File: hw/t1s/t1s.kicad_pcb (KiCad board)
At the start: 4 copper layers, 58 x 11.8 mm, 18 parts, among them J1 SFP_Module_Edge, J2 2-pin T1S (JST PH placeholder), U1 LIFCL-17 CrossLink-NX csfBGA-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, U2 STM32G031F6P6 (I2C slave: EEP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, U3 TPS62A01 3V3->1V0, U4 LDO 3V3->1V8, U5 LAN8670 (MII), U6 SPI flash (FPGA bitstream), Y1 25 MHz

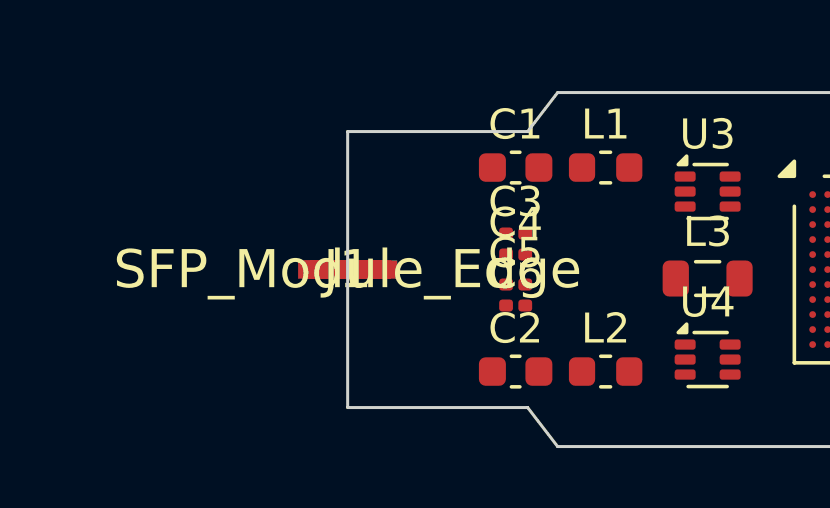
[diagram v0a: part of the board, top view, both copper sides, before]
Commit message: T1 module: schematic, routed 4-layer PCB, fab outputs, controller firmware
One netlist in make_t1.py drives both the schematic and the PCB pad nets;
the schematic's exported netlist matches it pin for pin (175 pins), and
eeschema's ERC is clean. Every block is from its datasheet: DP83TG720S
pins, straps, MDI network and decoupling; the DP83TC812S loadout differs
only in leaving FB3 off; TPS62821 1.0 V buck.

Routed by Freerouting 1.9.0 with In1 GND / In2 3V3 planes, outer GND
pours added after import, no pour among the gold fingers. KiCad DRC:
0 violations, 0 unconnected.

Firmware (STM32G031, 1.7 KB): A0h EEPROM emulation, I2C-to-MDIO bridge at
0x56 in the mdio-i2c protocol, TX_DISABLE holds the PHY in reset, RX_LOS
follows the link.

Not orderable yet: the H-MTD footprint is a placeholder and the SGMII
widths wait on the fab's stackup.
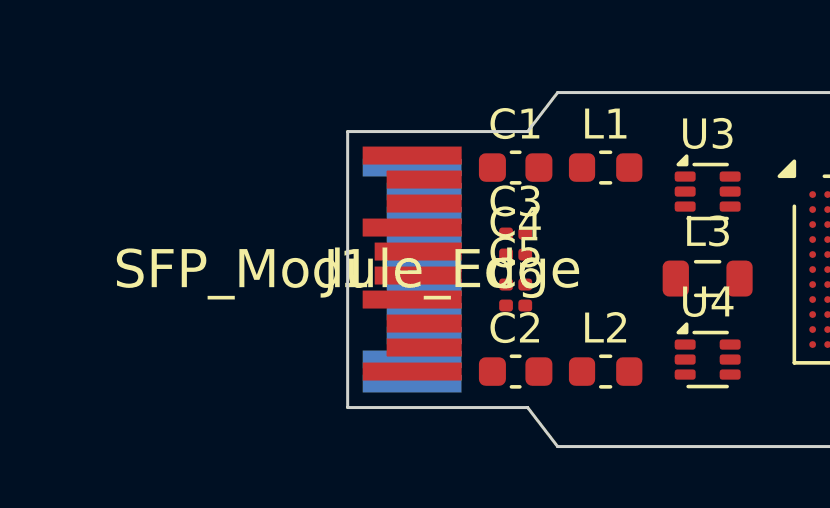
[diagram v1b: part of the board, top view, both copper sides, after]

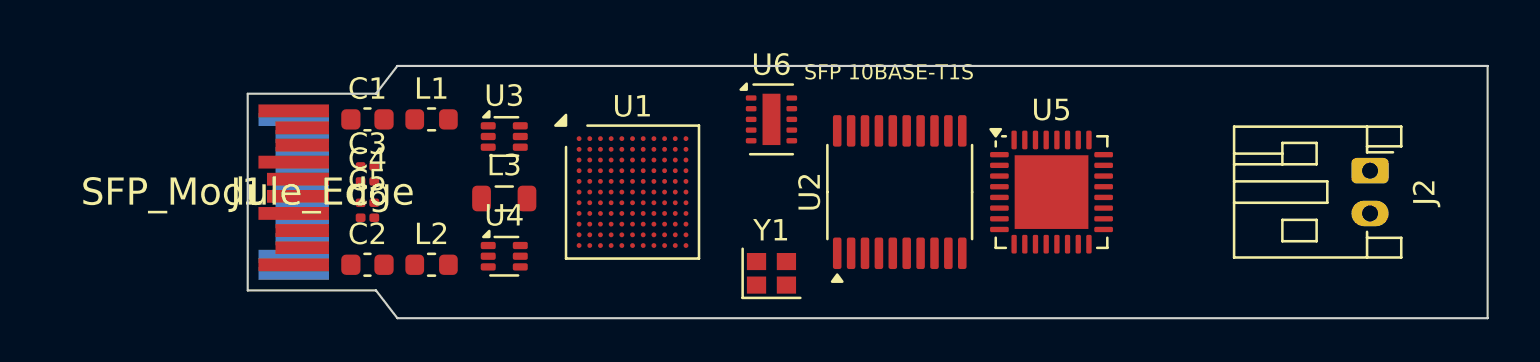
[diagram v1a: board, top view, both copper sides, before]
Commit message: RJ45: 6-layer board routed and clean, JLC panel and order sheet
- rj45: DRC 0 / 0 unconnected (KiCad 7 and 9), parity clean, ERC 0/0;
  gerbers, BOM/CPL, 1:1 print; 5-board panel with hand-placed tabs,
  checked with the board's own rules; ORDER.md with cost estimate
- sfpgen: side-pin power stubs clear the next pin's label (they shorted
  +3V3 to AVDD33 in the RJ45 schematic); project min via / hole clearance
  from the design
- t1: schematic regenerated with the stub fix, KiCad 9 re-checked
- CI: rj45 joins the KiCad 9 matrix
- t1s: work in progress (6 layers, not yet fully routed)
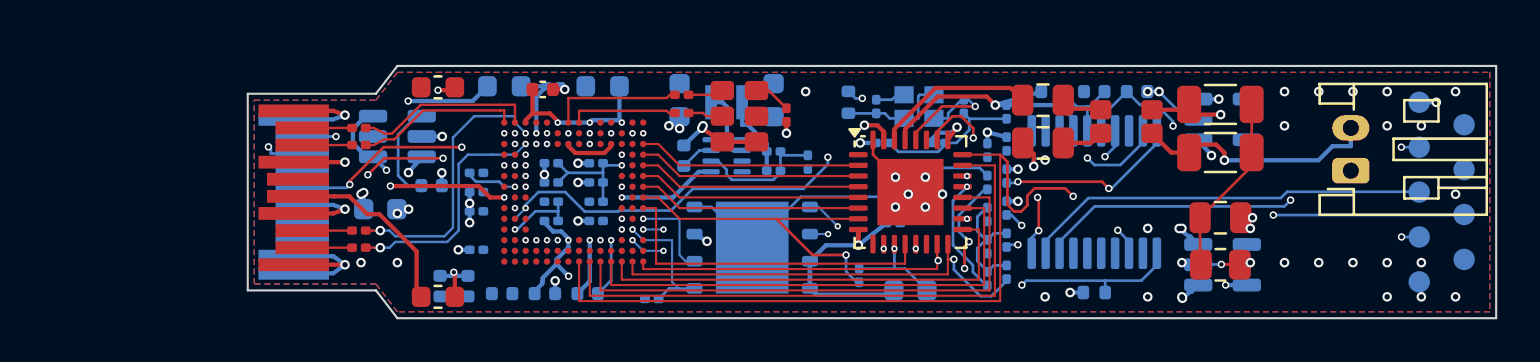
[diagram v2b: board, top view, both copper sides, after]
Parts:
- removed L3: 1uH, L_0805_2012Metric
- added C11: 4.7uF, Capacitor_SMD:C_0402_1005Metric, B.Cu at (120.4, 98.3)
- added C12: 10uF, Capacitor_SMD:C_0603_1608Metric, B.Cu at (124.6, 95.7)
- added C13: 10uF, Capacitor_SMD:C_0603_1608Metric, B.Cu at (120.2, 95.7)
- added C14: 120pF, Capacitor_SMD:C_0201_0603Metric, B.Cu at (124.6, 98.1)
- added C15: 1uF, Capacitor_SMD:C_0402_1005Metric, B.Cu at (111.9, 104.8)
- added C16: 1uF, Capacitor_SMD:C_0402_1005Metric, B.Cu at (113.9, 104.8)
- added C17: 1uF, Capacitor_SMD:C_0402_1005Metric, B.Cu at (115.9, 104.8)
- added C18: 4.7uF, Capacitor_SMD:C_0402_1005Metric, F.Cu at (113.8, 95.2)
- added C30: 18pF, Capacitor_SMD:C_0201_0603Metric, B.Cu at (129.4, 96.0)
- added C31: 18pF, Capacitor_SMD:C_0201_0603Metric, B.Cu at (133.5, 96.0)
- added C32: 100nF, Capacitor_SMD:C_0201_0603Metric, B.Cu at (129.7, 97.7)
- added C33: 100nF, Capacitor_SMD:C_0201_0603Metric, B.Cu at (132.3, 97.7)
- added C34: 100nF, Capacitor_SMD:C_0201_0603Metric, B.Cu at (130.2, 101.5)
- added C35: 100nF, Capacitor_SMD:C_0201_0603Metric, B.Cu at (135.5, 96.2)
- added C36: 2.2nF, Capacitor_SMD:C_0402_1005Metric, B.Cu at (108.6, 99.7)
- added C36A: 10uF, Capacitor_SMD:C_0603_1608Metric, B.Cu at (131.0, 104.6)
- added C37: 10uF, Capacitor_SMD:C_0603_1608Metric, B.Cu at (106.2, 100.8)
- added C40: 100nF 100V, Capacitor_SMD:C_0805_2012Metric, F.Cu at (137.2, 95.7)
- added C41: 100nF 100V, Capacitor_SMD:C_0805_2012Metric, F.Cu at (137.2, 97.7)
- added C42: 100nF 50V, Capacitor_SMD:C_0805_2012Metric, F.Cu at (145.5, 101.2)
- added C43: 100nF, Capacitor_SMD:C_0402_1005Metric, B.Cu at (137.6, 95.3)
- added C44: 1uF, Capacitor_SMD:C_0402_1005Metric, B.Cu at (139.6, 95.3)
- added C45: 100nF, Capacitor_SMD:C_0402_1005Metric, B.Cu at (141.6, 95.3)
- added C50: 100nF, Capacitor_SMD:C_0201_0603Metric, B.Cu at (114.2, 98.7)
- added C51: 100nF, Capacitor_SMD:C_0201_0603Metric, B.Cu at (116.3, 98.7)
- added C52: 100nF, Capacitor_SMD:C_0201_0603Metric, B.Cu at (114.2, 99.5)
- added C53: 100nF, Capacitor_SMD:C_0201_0603Metric, B.Cu at (116.3, 99.5)
- added C54: 100nF, Capacitor_SMD:C_0201_0603Metric, B.Cu at (114.2, 100.5)
- added C55: 100nF, Capacitor_SMD:C_0201_0603Metric, B.Cu at (116.3, 100.5)
- added C56: 100nF, Capacitor_SMD:C_0201_0603Metric, B.Cu at (114.2, 101.3)
- added C59: 100nF, Capacitor_SMD:C_0201_0603Metric, B.Cu at (114.3, 95.0)
- added C7: 100nF, Capacitor_SMD:C_0201_0603Metric, F.Cu at (120.3, 95.5)
- added C8: 100nF, Capacitor_SMD:C_0201_0603Metric, F.Cu at (120.3, 96.3)
- added C9: 100nF, Capacitor_SMD:C_0201_0603Metric, F.Cu at (125.2, 96.4)
- added FB1: BLM18KG601SH1, Inductor_SMD:L_0603_1608Metric, F.Cu at (108.9, 95.1)
- added FB2: BLM18KG601SH1, Inductor_SMD:L_0603_1608Metric, F.Cu at (108.9, 104.9)
- added FB3: BLM18KG601SH1, Inductor_SMD:L_0603_1608Metric, B.Cu at (116.6, 95.0)
- added FB4: BLM18KG601SH1, Inductor_SMD:L_0603_1608Metric, B.Cu at (112.0, 95.0)
- added R1: 4.7k, Resistor_SMD:R_0201_0603Metric, B.Cu at (110.7, 102.7)
- added R10: 10k, Resistor_SMD:R_0201_0603Metric, B.Cu at (134.6, 98.0)
- added R11: 10k, Resistor_SMD:R_0201_0603Metric, B.Cu at (134.6, 99.5)
- added R12: 10k, Resistor_SMD:R_0201_0603Metric, B.Cu at (135.5, 102.2)
- added R13: 10k, Resistor_SMD:R_0201_0603Metric, B.Cu at (135.5, 103.8)
- added R14: 10k, Resistor_SMD:R_0201_0603Metric, B.Cu at (134.6, 101.0)
- added R15: 10k, Resistor_SMD:R_0201_0603Metric, B.Cu at (134.6, 102.5)
- added R16: 10k, Resistor_SMD:R_0201_0603Metric, B.Cu at (134.6, 104.0)
- added R17: 10k, Resistor_SMD:R_0201_0603Metric, B.Cu at (128.6, 103.9)
- added R18: 10k, Resistor_SMD:R_0201_0603Metric, B.Cu at (135.5, 97.8)
- added R19: 10k, Resistor_SMD:R_0201_0603Metric, B.Cu at (135.5, 99.2)
- added R20: 10k, Resistor_SMD:R_0201_0603Metric, B.Cu at (135.5, 100.8)
- added R21: 12.4k 1%, Resistor_SMD:R_0402_1005Metric, B.Cu at (128.1, 95.8)
- added R22: 49.9 1%, Resistor_SMD:R_1206_3216Metric, F.Cu at (145.5, 95.9)
- added R23: 49.9 1%, Resistor_SMD:R_1206_3216Metric, F.Cu at (145.5, 98.2)
- added R24: 100k, Resistor_SMD:R_0805_2012Metric, F.Cu at (145.5, 103.4)
- added R25: 10k, Resistor_SMD:R_0402_1005Metric, B.Cu at (139.6, 104.7)
- added R3: 4.7k, Resistor_SMD:R_0201_0603Metric, B.Cu at (110.7, 100.9)
- added R4: 4.7k, Resistor_SMD:R_0201_0603Metric, B.Cu at (110.7, 100.0)
- added R5: 4.7k, Resistor_SMD:R_0201_0603Metric, B.Cu at (116.3, 101.3)
- added R6: 4.7k, Resistor_SMD:R_0201_0603Metric, B.Cu at (118.9, 105.0)
- added R7: 4.7k, Resistor_SMD:R_0201_0603Metric, B.Cu at (110.7, 99.1)
- added R8: 57.6k 1%, Resistor_SMD:R_0201_0603Metric, B.Cu at (124.6, 99.0)
- added R9: 100k 1%, Resistor_SMD:R_0201_0603Metric, B.Cu at (126.2, 98.6)
- added TP1: +3V3, TestPoint:TestPoint_Pad_D1.0mm, B.Cu at (154.8, 95.8)
- added TP10: JTAG_TCK, TestPoint:TestPoint_Pad_D1.0mm, B.Cu at (156.9, 96.8)
- added TP11: JTAG_TMS, TestPoint:TestPoint_Pad_D1.0mm, B.Cu at (156.9, 99.0)
- added TP12: JTAG_TDI, TestPoint:TestPoint_Pad_D1.0mm, B.Cu at (156.9, 101.0)
- added TP13: JTAG_TDO, TestPoint:TestPoint_Pad_D1.0mm, B.Cu at (156.9, 103.2)
- added TP2: SWDIO, TestPoint:TestPoint_Pad_D1.0mm, B.Cu at (154.8, 97.9)
- added TP3: SWCLK, TestPoint:TestPoint_Pad_D1.0mm, B.Cu at (154.8, 100.0)
- added TP4: NRST, TestPoint:TestPoint_Pad_D1.0mm, B.Cu at (154.8, 102.1)
- added TP5: GND, TestPoint:TestPoint_Pad_D1.0mm, B.Cu at (154.8, 104.2)
- added U7: TLV75512PDBVR, Package_TO_SOT_SMD:SOT-23-5, B.Cu at (145.6, 103.4)
- added U8: STM32G031F6P6, Package_SO:TSSOP-20_4.4x6.5mm_P0.65mm, B.Cu at (139.6, 100.0)
- added X1: OB2EL89CLIB112YLC-125M, sfp:Oscillator_YXC_3225-6Pin_LVDS, F.Cu at (123.0, 96.5)
- C1: value 10uF VccT -> 1uF; footprint C_0603_1608Metric -> Capacitor_SMD:C_0402_1005Metric; moved to B.Cu
- C2: value 10uF VccR -> 100nF; footprint C_0603_1608Metric -> Capacitor_SMD:C_0402_1005Metric; moved to B.Cu
- C3: value 100nF TD+ -> 100nF; footprint C_0201_0603Metric -> Capacitor_SMD:C_0201_0603Metric
- C4: value 100nF TD- -> 100nF; footprint C_0201_0603Metric -> Capacitor_SMD:C_0201_0603Metric
- C5: value 100nF RD+ -> 100nF; footprint C_0201_0603Metric -> Capacitor_SMD:C_0201_0603Metric
- C6: value 100nF RD- -> 100nF; footprint C_0201_0603Metric -> Capacitor_SMD:C_0201_0603Metric
- J1: value SFP_Module_Edge -> SFP edge (INF-8074i)
- J2: value 2-pin T1S (JST PH placeholder) -> S2B-PH-K-S; footprint JST_PH_S2B-PH-K_1x02_P2.00mm_Horizontal -> Connector_JST:JST_PH_S2B-PH-K_1x02_P2.00mm_Horizontal
- L1: value ferrite VccT -> 470nH DFE201610E-R47M; footprint L_0603_1608Metric -> Inductor_SMD:L_Murata_DFE201610P; moved to B.Cu
- L2: value ferrite VccR -> ACT1210E-241-2P; footprint L_0603_1608Metric -> sfp:L_CommonMode_3225
- U1: value LIFCL-17 CrossLink-NX csfBGA-121 6x6 -> GW5AT-LV15MG132C1/I0; footprint ST_UFBGA-121_6x6mm_Layout11x11_P0.5mm -> sfp:Gowin_MBGA-132_8x8mm_P0.5mm
- U2: value STM32G031F6P6 (I2C slave: EEPROM A0/A2 + MDIO bridge 0x56) -> GD25Q64CWIGR; footprint TSSOP-20_4.4x6.5mm_P0.65mm -> Package_SON:WSON-8-1EP_6x5mm_P1.27mm_EP3.4x4.3mm; moved to B.Cu
- U3: value TPS62A01 3V3->1V0 -> TPS62822DLC; footprint SOT-563 -> sfp:Texas_VSON-HR-8_1.5x2mm_P0.5mm; moved to B.Cu
- U4: value LDO 3V3->1V8 -> TPS22918DBVR; footprint SOT-563 -> Package_TO_SOT_SMD:SOT-23-6; moved to B.Cu
- U5: value LAN8670 (MII) -> LAN8670C2-E/LMX; footprint QFN-32-1EP_5x5mm_P0.5mm_EP3.45x3.45mm -> Package_DFN_QFN:VQFN-32-1EP_5x5mm_P0.5mm_EP3.1x3.1mm
- U6: value SPI flash (FPGA bitstream) -> TLV75518PDBVR; footprint WSON-10-1EP_2x3mm_P0.5mm_EP0.84x2.4mm -> Package_TO_SOT_SMD:SOT-23-5; moved to B.Cu
- Y1: value 25 MHz -> 25MHz CL12pF 2016; footprint Crystal_SMD_2016-4Pin_2.0x1.6mm -> Crystal:Crystal_SMD_2016-4Pin_2.0x1.6mm; moved to B.Cu
- moved L2 33.2 mm to (141.1, 96.7)
- moved U6 21.1 mm to (145.6, 96.6)
- moved L1 13.8 mm to (122.4, 95.8)
- moved U3 10.4 mm to (122.4, 98.3)
- moved Y1 10.4 mm to (131.4, 96.0)
- moved C1 8.51 mm to (109.0, 104.4), turned to -90 degrees
- moved U4 7.51 mm to (107.0, 97.4)
- moved U2 7.37 mm to (123.6, 102.6), turned to 0 degrees
- moved U5 6.60 mm to (131.0, 100.0)
- moved C2 4.81 mm to (110.3, 104.4), turned to -90 degrees
- moved U1 2.75 mm to (115.2, 100.0)
- moved C4 2.53 mm to (105.2, 97.0)
- moved C6 1.46 mm to (105.2, 102.6)
- moved C5 1.36 mm to (105.2, 101.8)
- moved C3 1.08 mm to (105.2, 97.8)
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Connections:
- C1 pad 1: (no net) -> VIN_RAW
- C1 pad 2: (no net) -> GND
- C2 pad 1: (no net) -> VIN_RAW
- C2 pad 2: (no net) -> GND
- C3 pad 1: (no net) -> TD_P
- C3 pad 2: (no net) -> SRX_M
- C4 pad 1: (no net) -> TD_N
- C4 pad 2: (no net) -> SRX_P
- C5 pad 1: (no net) -> RD_P
- C5 pad 2: (no net) -> STX_P
- C6 pad 1: (no net) -> RD_N
- C6 pad 2: (no net) -> STX_M
- J1 pad 1: (no net) -> GND
- J1 pad 10: (no net) -> GND
- J1 pad 11: (no net) -> GND
- J1 pad 12: (no net) -> RD_N
- J1 pad 13: (no net) -> RD_P
- J1 pad 14: (no net) -> GND
- J1 pad 15: (no net) -> VCCR
- J1 pad 16: (no net) -> VCCT
- J1 pad 17: (no net) -> GND
- J1 pad 18: (no net) -> TD_P
- J1 pad 19: (no net) -> TD_N
- J1 pad 2: (no net) -> TX_FAULT
- J1 pad 20: (no net) -> GND
- J1 pad 3: (no net) -> TX_DISABLE
- J1 pad 4: (no net) -> SDA
- J1 pad 5: (no net) -> SCL
- J1 pad 6: (no net) -> GND
- J1 pad 7: (no net) -> unconnected-(J1-RS0-Pad7)
- J1 pad 8: (no net) -> RX_LOS
- J1 pad 9: (no net) -> GND
- J2 pad 1: (no net) -> MDI_P
- J2 pad 2: (no net) -> MDI_N
- L1 pad 1: (no net) -> BUCK_SW
- L1 pad 2: (no net) -> VCC_CORE
- L2 pad 1: (no net) -> MDI_CP
- L2 pad 2: (no net) -> MDI_CN
- U1 pad A1: (no net) -> SRX_M
- U1 pad A10: (no net) -> unconnected-(U1-Q0_LN2_RXP_I-PadA10)
- U1 pad A11: (no net) -> unconnected-(U1-Q0_LN2_RXM_I-PadA11)
- U1 pad A2: (no net) -> SRX_P
- U1 pad A3: (no net) -> VDDAQ
- U1 pad A4: (no net) -> unconnected-(U1-Q0_LN1_RXP_I-PadA4)
- U1 pad A5: (no net) -> unconnected-(U1-Q0_LN1_RXM_I-PadA5)
- U1 pad A6: (no net) -> VDDAQ
- U1 pad A7: (no net) -> REFCLK_M
- U1 pad A8: (no net) -> REFCLK_P
- U1 pad A9: (no net) -> VDDAQ
- U1 pad B1: (no net) -> GND
- U1 pad B10: (no net) -> unconnected-(U1-Q0_REFCLKM_1-PadB10)
- U1 pad B11: (no net) -> GND
- U1 pad B2: (no net) -> VCC_CORE
- U1 pad B3: (no net) -> STX_P
- U1 pad B4: (no net) -> VDDTQ
- U1 pad B5: (no net) -> GND
- U1 pad B6: (no net) -> unconnected-(U1-Q0_LN1_TXP_O-PadB6)
- U1 pad B7: (no net) -> GND
- U1 pad B8: (no net) -> unconnected-(U1-Q0_LN2_TXP_O-PadB8)
- U1 pad B9: (no net) -> GND
- U1 pad C1: (no net) -> unconnected-(U1-M1_D2A-PadC1)
- U1 pad C10: (no net) -> unconnected-(U1-Q0_REFCLKP_1-PadC10)
- U1 pad C11: (no net) -> VDDHAQ
- U1 pad C2: (no net) -> +3V3
- U1 pad C3: (no net) -> STX_M
- U1 pad C4: (no net) -> +3V3
- U1 pad C5: (no net) -> VCC_CORE
- U1 pad C6: (no net) -> unconnected-(U1-Q0_LN1_TXM_O-PadC6)
- U1 pad C7: (no net) -> VDDHAQ
- U1 pad C8: (no net) -> unconnected-(U1-Q0_LN2_TXM_O-PadC8)
- U1 pad C9: (no net) -> VCC_CORE
- U1 pad D1: (no net) -> unconnected-(U1-M1_D2C-PadD1)
- U1 pad D2: (no net) -> unconnected-(U1-M1_D2B-PadD2)
- U1 pad D3: (no net) -> GND
- U1 pad E1: (no net) -> +3V3
- U1 pad E2: (no net) -> VCC_CORE
- U1 pad E3: (no net) -> VCC_CORE
- U1 pad F1: (no net) -> unconnected-(U1-M1_D0B-PadF1)
- U1 pad F2: (no net) -> unconnected-(U1-M1_D0A-PadF2)
- U1 pad F3: (no net) -> +3V3
- U1 pad G1: (no net) -> unconnected-(U1-M1_D0C-PadG1)
- U1 pad G2: (no net) -> JTAG_TCK
- U1 pad G3: (no net) -> JTAG_TMS
- U1 pad H1: (no net) -> VCC_CORE
- U1 pad H2: (no net) -> unconnected-(U1-IOL22B-PadH2)
- U1 pad H3: (no net) -> unconnected-(U1-IOL22A-PadH3)
- U1 pad J1: (no net) -> unconnected-(U1-M1_D1C-PadJ1)
- U1 pad J2: (no net) -> JTAG_TDO
- U1 pad J3: (no net) -> JTAG_TDI
- U1 pad K1: (no net) -> unconnected-(U1-M1_D1B-PadK1)
- U1 pad K2: (no net) -> unconnected-(U1-IOL26B-PadK2)
- U1 pad K3: (no net) -> unconnected-(U1-IOL26A-PadK3)
- U1 pad L1: (no net) -> unconnected-(U1-M1_D1A-PadL1)
- U1 pad L2: (no net) -> GND
- U1 pad L3: (no net) -> unconnected-(U1-IOL29A-PadL3)
- U2 pad 1: (no net) -> F_CS_N
- U2 pad 2: (no net) -> F_MISO
- U2 pad 3: (no net) -> +3V3
- U2 pad 4: (no net) -> GND
- U2 pad 5: (no net) -> F_MOSI
- U2 pad 6: (no net) -> F_CLK
- U2 pad 7: (no net) -> +3V3
- U2 pad 8: (no net) -> +3V3
- U2 pad 9: (no net) -> GND
- U3 pad 1: (no net) -> +3V3
- U3 pad 2: (no net) -> BUCK_FB
- U3 pad 3: (no net) -> GND
- U3 pad 4: (no net) -> unconnected-(U3-NC-Pad4)
- U3 pad 5: (no net) -> GND
- U3 pad 6: (no net) -> BUCK_SW
- U4 pad 1: (no net) -> VIN_RAW
- U4 pad 2: (no net) -> GND
- U4 pad 3: (no net) -> VIN_RAW
- U4 pad 4: (no net) -> SS_CT
- U4 pad 5: (no net) -> +3V3
- U4 pad 6: (no net) -> +3V3
- U5 pad 1: (no net) -> unconnected-(U5-DNC-Pad1)
- U5 pad 10: (no net) -> PHY_RST_N
- U5 pad 11: (no net) -> GND
- U5 pad 12: (no net) -> TXCLK
- U5 pad 13: (no net) -> MDC
- U5 pad 14: (no net) -> MDIO
- U5 pad 15: (no net) -> CRS
- U5 pad 16: (no net) -> RXD0
- U5 pad 17: (no net) -> RXCLK
- U5 pad 18: (no net) -> +3V3
- U5 pad 19: (no net) -> RXD1
- U5 pad 2: (no net) -> COL
- U5 pad 20: (no net) -> RXDV
- U5 pad 21: (no net) -> RXER
- U5 pad 22: (no net) -> PHY_INT_N
- U5 pad 23: (no net) -> RXD2
- U5 pad 24: (no net) -> RXD3
- U5 pad 25: (no net) -> +3V3
- U5 pad 26: (no net) -> RBIAS
- U5 pad 27: (no net) -> XTI
- U5 pad 28: (no net) -> XTO
- U5 pad 29: (no net) -> +3V3
- U5 pad 3: (no net) -> TXD3
- U5 pad 30: (no net) -> TRXP
- U5 pad 31: (no net) -> TRXN
- U5 pad 32: (no net) -> GND
- U5 pad 33: (no net) -> GND
- U5 pad 4: (no net) -> TXD2
- U5 pad 5: (no net) -> TXD1
- U5 pad 6: (no net) -> TXD0
- U5 pad 7: (no net) -> TXEN
- U5 pad 8: (no net) -> +3V3
- U5 pad 9: (no net) -> unconnected-(U5-DNC-Pad9)
- U6 pad 1: (no net) -> +3V3
- U6 pad 2: (no net) -> GND
- U6 pad 3: (no net) -> +3V3
- U6 pad 4: (no net) -> unconnected-(U6-NC-Pad4)
- U6 pad 5: (no net) -> VDDHAQ
- Y1 pad 1: (no net) -> XTI
- Y1 pad 2: (no net) -> GND
- Y1 pad 3: (no net) -> XTO
- Y1 pad 4: (no net) -> GND
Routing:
- net GND: track 0.00 -> 86.5 mm, vias 0 -> 61
- net TX_FAULT: track 0.00 -> 61.7 mm, vias 0 -> 4
- net +3V3: track 0.00 -> 57.3 mm, vias 0 -> 39
- net JTAG_TDI: track 0.00 -> 49.8 mm, vias 0 -> 3
- net RXD3: track 0.00 -> 48.2 mm, vias 0 -> 3
- net TX_DISABLE: track 0.00 -> 47.8 mm, vias 0 -> 2
- net SCL: track 0.00 -> 42.8 mm, vias 0 -> 4
- net V1P2: track 0.00 -> 37.5 mm, vias 0 -> 3
- net RXD2: track 0.00 -> 28.2 mm
- net RXDV: track 0.00 -> 25.2 mm
- net RXD1: track 0.00 -> 23.2 mm
- net RXD0: track 0.00 -> 20.9 mm, vias 0 -> 1
- net RXCLK: track 0.00 -> 20.7 mm
- net CRS: track 0.00 -> 20.1 mm, vias 0 -> 2
- net SWDIO: track 0.00 -> 19.4 mm, vias 0 -> 2
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- added copper zone on In3.Cu, net +3V3
- added copper zone on B.Cu, net GND
- added copper zone on F.Cu, net GND
- added copper zone on In1.Cu, net GND
- added copper zone on In4.Cu, net GND
- added copper zone on In2.Cu, net VCC_CORE
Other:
- board size 58 x 11.8 mm -> 58.4 x 11.8 mm
- copper layers 4 -> 6
- board text added: "T1S SFP"
- board text removed: "SFP 10BASE-T1S"
- board text removed: "inside cage: top <= 4.65 mm, bottom <= 1.65 mm"

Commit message: T1S: 6-layer board routed and clean, JLC panel and order sheet
- DRC 0 / 0 unconnected (KiCad 7 and 9), schematic parity clean, ERC 0
  errors; gerbers, BOM/CPL, 1:1 print; 5-board panel, DRC clean with the
  board's rules
- the core rail is an In4 island (on In2 it walled the ball field in); In2
  carries two hand-laid buses to the MCU, found once by a maze search and
  baked into make_t1s.py (IN2_BUS)
- JTAG pads beside the FPGA, flash turned 180 degrees, strap/XTO/+3V3 vias in
  the PHY's pads, the MDI pair swapped at the PHY (DME is polarity-free),
  L3/M12 reconnected (they had slipped into a comment)
- MCU pins follow the buses: TX_DISABLE / TX_FAULT on PC14 / PC15 (fw)
- sfpgen: side-pin power stubs no longer turn (GND on TXCLK merged half
  the FPGA's nets in the schematic); ISLANDS as outlines; router vias that
  double a plane dogbone are dropped; T1/RJ45 schematics regenerated,
  both still pass ERC and KiCad 9
- CI: t1s joins the KiCad 9 matrix
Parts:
- removed C36A: 10uF, Capacitor_SMD:C_0603_1608Metric
- added C60: 10uF, Capacitor_SMD:C_0603_1608Metric, F.Cu at (127.6, 95.5)
- R25: footprint Resistor_SMD:R_0402_1005Metric -> Resistor_SMD:R_0201_0603Metric
- TP10, TP11, TP12, TP13: footprint TestPoint:TestPoint_Pad_D1.0mm -> sfp:TestPoint_Pad_D1.0mm_NoSilk; moved to F.Cu
- moved TP10 46.7 mm to (110.3, 100.0)
- moved TP13 46.6 mm to (110.3, 101.2)
- moved TP12 46.6 mm to (110.3, 102.4)
- moved TP11 46.6 mm to (110.3, 98.8)
- moved C15 35.3 mm to (146.7, 98.8)
- moved C16 34.3 mm to (148.2, 103.9), turned to -90 degrees
- moved R25 31.2 mm to (109.2, 98.1), turned to -90 degrees
- moved R3 29.5 mm to (140.0, 104.7), turned to 90 degrees
- moved R4 28.9 mm to (139.2, 104.7), turned to 90 degrees
- moved R6 5.37 mm to (119.4, 99.7), turned to -90 degrees
- moved C36 4.64 mm to (109.5, 95.2)
- moved FB1 4.11 mm to (107.6, 99.0)
- moved R12 3.05 mm to (132.8, 103.8), turned to 90 degrees
- moved R11 2.15 mm to (134.6, 97.4)
- moved R15 2.05 mm to (134.6, 100.5), turned to 90 degrees
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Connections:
- C30 pad 1: XTI -> XTO
- C31 pad 1: XTO -> XTI
- C54 pad 1: VDDAQ -> VCC_CORE
- U1 pad L3: unconnected-(U1-IOL29A-PadL3) -> FPGA_DONE
- U1 pad M12: unconnected-(U1-IOB9A-PadM12) -> FPGA_READY
- U5 pad 30: TRXP -> TRXN
- U5 pad 31: TRXN -> TRXP
- U8 pad 11: TX_DISABLE -> unconnected-(U8-PA4-Pad11)
- U8 pad 13: TX_FAULT -> unconnected-(U8-PA6-Pad13)
- U8 pad 2: unconnected-(U8-PC14/PB9-Pad2) -> TX_DISABLE
- U8 pad 3: unconnected-(U8-PC15-Pad3) -> TX_FAULT
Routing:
- net JTAG_TDI: track 49.8 -> 3.91 mm, vias 3 -> 2
- net RX_LOS: track 0.00 -> 41.9 mm, vias 0 -> 2
- net SDA: track 0.00 -> 39.7 mm, vias 0 -> 2
- net VDDHAQ: track 2.47 -> 37.0 mm, vias 0 -> 4
- net FPGA_LINK: track 0.00 -> 31.0 mm, vias 0 -> 2
- net FPGA_DONE: track 0.00 -> 30.1 mm, vias 0 -> 2
- net FPGA_RECONFIG_N: track 0.00 -> 29.6 mm, vias 1 -> 2
- net TX_FAULT: track 61.7 -> 39.2 mm, vias 4 -> 2
- net RXD3: track 48.2 -> 31.0 mm, vias 3 -> 1
- net MDIO: track 0.21 -> 16.8 mm, vias 0 -> 2
- net VCC_CORE: track 19.1 -> 10.00 mm, vias 13 -> 17
- net F_MOSI: track 12.6 -> 4.27 mm, vias 3 -> 1
- net RXER: track 5.80 -> 12.9 mm
- net TX_DISABLE: track 47.8 -> 41.0 mm
- net GND: track 86.5 -> 79.8 mm, vias 61 -> 66
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- added copper zone on In4.Cu, net VCC_CORE
- removed copper zone on In2.Cu, net VCC_CORE

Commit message: References checked against the design; the fixes they turned up
docs/REFERENCES.md: the standards, Linux drivers, TI / Realtek / Microchip /
Gowin datasheets, app notes and EVMs, and commercial modules, each with a
table of the design against it.

Fixed from it:
- T1S: CLKHOLD_N (K3) tied high - pulled down during configuration, it would
  have held the flash clock and the FPGA would never load; P1 (also
  SSPI_CS_N) pulled up (R26); AN1718 BIN: 0.75 W end-node resistors (were
  0.25 W), 100 V centre cap (was 50 V), no copper under the CMC
- RJ45 / T1S: buck inductor 1.0 uH (TPS6282x Table 3): the RTL8221B wants
  its core switcher out of pulse skipping, which now starts at ~0.15 A, not
  ~0.33 A
- T1: no copper under the CMC on F/In1 (DP83TG720 8.5); the TC812 loadout
  fits the 200 uH CMC its datasheet asks for
- fw: PHY settings 70 ms after reset release (TG720: 65 ms before the first
  MDIO frame) with the 0x56 bridge answering 0xFFFF until then; LAN8670 set-up
  picked by silicon revision (AN1699 Rev G: C2 or D0); collision detection
  follows PLCA as AN1699 asks

All three boards: DRC 0 / 0 unconnected, KiCad 9 PASS, panels clean.
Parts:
- added R26: 4.7k, Resistor_SMD:R_0201_0603Metric, B.Cu at (140.8, 104.7)
- C42: value 100nF 50V -> 100nF 100V
- L1: value 470nH DFE201610E-R47M -> 1uH DFE201610E-1R0M
- R22, R23: value 49.9 1% -> 49.9 1% 0.75W
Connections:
- U1 pad K3: unconnected-(U1-IOL26A-PadK3) -> +3V3
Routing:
- net +3V3: track 54.6 -> 55.6 mm, vias 33 -> 35

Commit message: Review fixes: 100 V MDI DC block, 128 Mbit flash, T1S MDI geometry
- T1 C33/C34: 100 nF 100 V X5R 0402 (GRM155R62A104KE14D, C162178), split
  from the 16 V decap line (C1525) they had been grouped with
- T1 R6/R7: 1 k 1 % 0.2 W anti-surge 0402 (C313354) instead of 62.5 mW;
  still short of TI's 0.75 W 2010, documented
- T1S U2: GD25Q128EWIGR (C2982923), same WSON-8 footprint, so Gowin's
  default golden address 0x800000 is inside the part; ORDER.md gives the
  flash layout
- compliance.py: each lane's geometry comes from its routed track width;
  the T1S MDI is two 0.2 mm lines (Z0 44.8) with its own delay and loss,
  and an unsolved width now stops the run
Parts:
- U2: value GD25Q64CWIGR -> GD25Q128EWIGR

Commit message: T1S routed on the corrected SFP edge: DRC 0 / 0, KiCad 9 PASS, panel 0 errors
Freerouting for the slow nets around the hand-laid copper of 4687dd1, best
of two trials kept as t1s.ses (rebuild with --reuse-ses). Two links the
router left open, now laid before routing so any session gets them:
- a +3V3 via on C43's track for the MCU's VDD pin and its decaps (the old
  via sat where L2's current CMC land is);
- R8 / C14's core ends into In4's VCC_CORE island through their own via.

- KiCad 7: DRC 0 violations, 0 unconnected; ERC 0 errors (2 library-copy
  warnings, the LDOs, as before)
- KiCad 9: DRC 0 errors, 0 unconnected, parity clean, ERC 0 errors
- panel: 0 errors, 0 unconnected (library warnings only)
- edge: all 20 fingers as SFF-8419 figure 7-2, nets included
  (docs/COMPLIANCE.md section 3, positions stated independently)
- pairs: SRX 13.76/12.99 mm, no vias; STX 8.51/8.04 mm, 2/2 vias;
  both P to P

README: the edge-mirror warning is resolved for all three boards. T1S
stays "do not order" for its own reason - no transceiver IP, synthesis,
timing or bitstream yet.
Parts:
- C36: moved to F.Cu
- C37: footprint Capacitor_SMD:C_0603_1608Metric -> Capacitor_SMD:C_0402_1005Metric; moved to F.Cu
- U5: footprint Package_DFN_QFN:VQFN-32-1EP_5x5mm_P0.5mm_EP3.1x3.1mm -> Package_DFN_QFN:VQFN-32-1EP_5x5mm_P0.5mm_EP3.5x3.5mm
- moved R25 33.1 mm to (141.6, 104.7), turned to 90 degrees
- moved C36 8.76 mm to (110.0, 103.9)
- moved C4 6.00 mm to (105.2, 103.0)
- moved FB2 5.99 mm to (107.4, 99.1)
- moved U4 5.85 mm to (108.7, 103.0), turned to -90 degrees
- moved C1 5.76 mm to (107.3, 98.9), turned to 0 degrees
- moved C2 5.61 mm to (109.2, 98.9), turned to 0 degrees
- moved C6 5.20 mm to (105.2, 97.4)
- moved C3 4.40 mm to (105.2, 102.2)
- moved C37 3.76 mm to (108.0, 104.1), turned to 180 degrees
- moved C5 3.60 mm to (105.2, 98.2)
- moved FB1 1.76 mm to (107.4, 100.8)
- moved R1 0.94 mm to (111.1, 103.5), turned to 90 degrees
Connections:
- C3 pad 2: SRX_M -> SRX_P
- C4 pad 2: SRX_P -> SRX_M
- R1 pad 2: MODE1 -> MODE
- U1 pad N1: MODE1 -> MODE
- U1 pad N2: unconnected-(U1-IOL31B-PadN2) -> MODE
- U8 pad 1: SDA -> SCL
- U8 pad 11: unconnected-(U8-PA4-Pad11) -> TX_FAULT
- U8 pad 12: RX_LOS -> unconnected-(U8-PA5-Pad12)
- U8 pad 13: unconnected-(U8-PA6-Pad13) -> TX_DISABLE
- U8 pad 17: unconnected-(U8-PA12/PA10-Pad17) -> SDA
- U8 pad 2: TX_DISABLE -> unconnected-(U8-PC14/PB9-Pad2)
- U8 pad 20: SCL -> unconnected-(U8-PB3/PB4/PB5/PB6-Pad20)
- U8 pad 3: TX_FAULT -> RX_LOS
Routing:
- net MDC: track 12.3 -> 29.4 mm, vias 3 -> 2
- net MDI_N: track 10.6 -> 22.9 mm
- net TX_FAULT: track 39.2 -> 50.8 mm, vias 2 -> 3
- net VIN_RAW: track 21.7 -> 10.4 mm, vias 3 -> 1
- net SRX_M: track 7.67 -> 13.0 mm
- net SRX_P: track 8.44 -> 13.8 mm
- net VCCR: track 9.70 -> 4.55 mm
- net RXER: track 12.9 -> 7.84 mm, vias 1 -> 2
- net MDI_P: track 14.9 -> 10.4 mm
- net STX_P: track 12.9 -> 8.51 mm
- net GND: track 79.8 -> 76.2 mm, vias 66 -> 70
- net STX_M: track 11.3 -> 8.04 mm
- net SS_CT: track 1.67 -> 4.86 mm, vias 0 -> 1
- net +3V3: track 55.6 -> 58.3 mm, vias 35 -> 33
- net RBIAS: track 9.91 -> 7.40 mm
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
